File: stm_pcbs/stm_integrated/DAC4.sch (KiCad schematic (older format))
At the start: 21 parts, among them P4 BNC, U10 AD8676, U11 AD5791, U12 AD8675

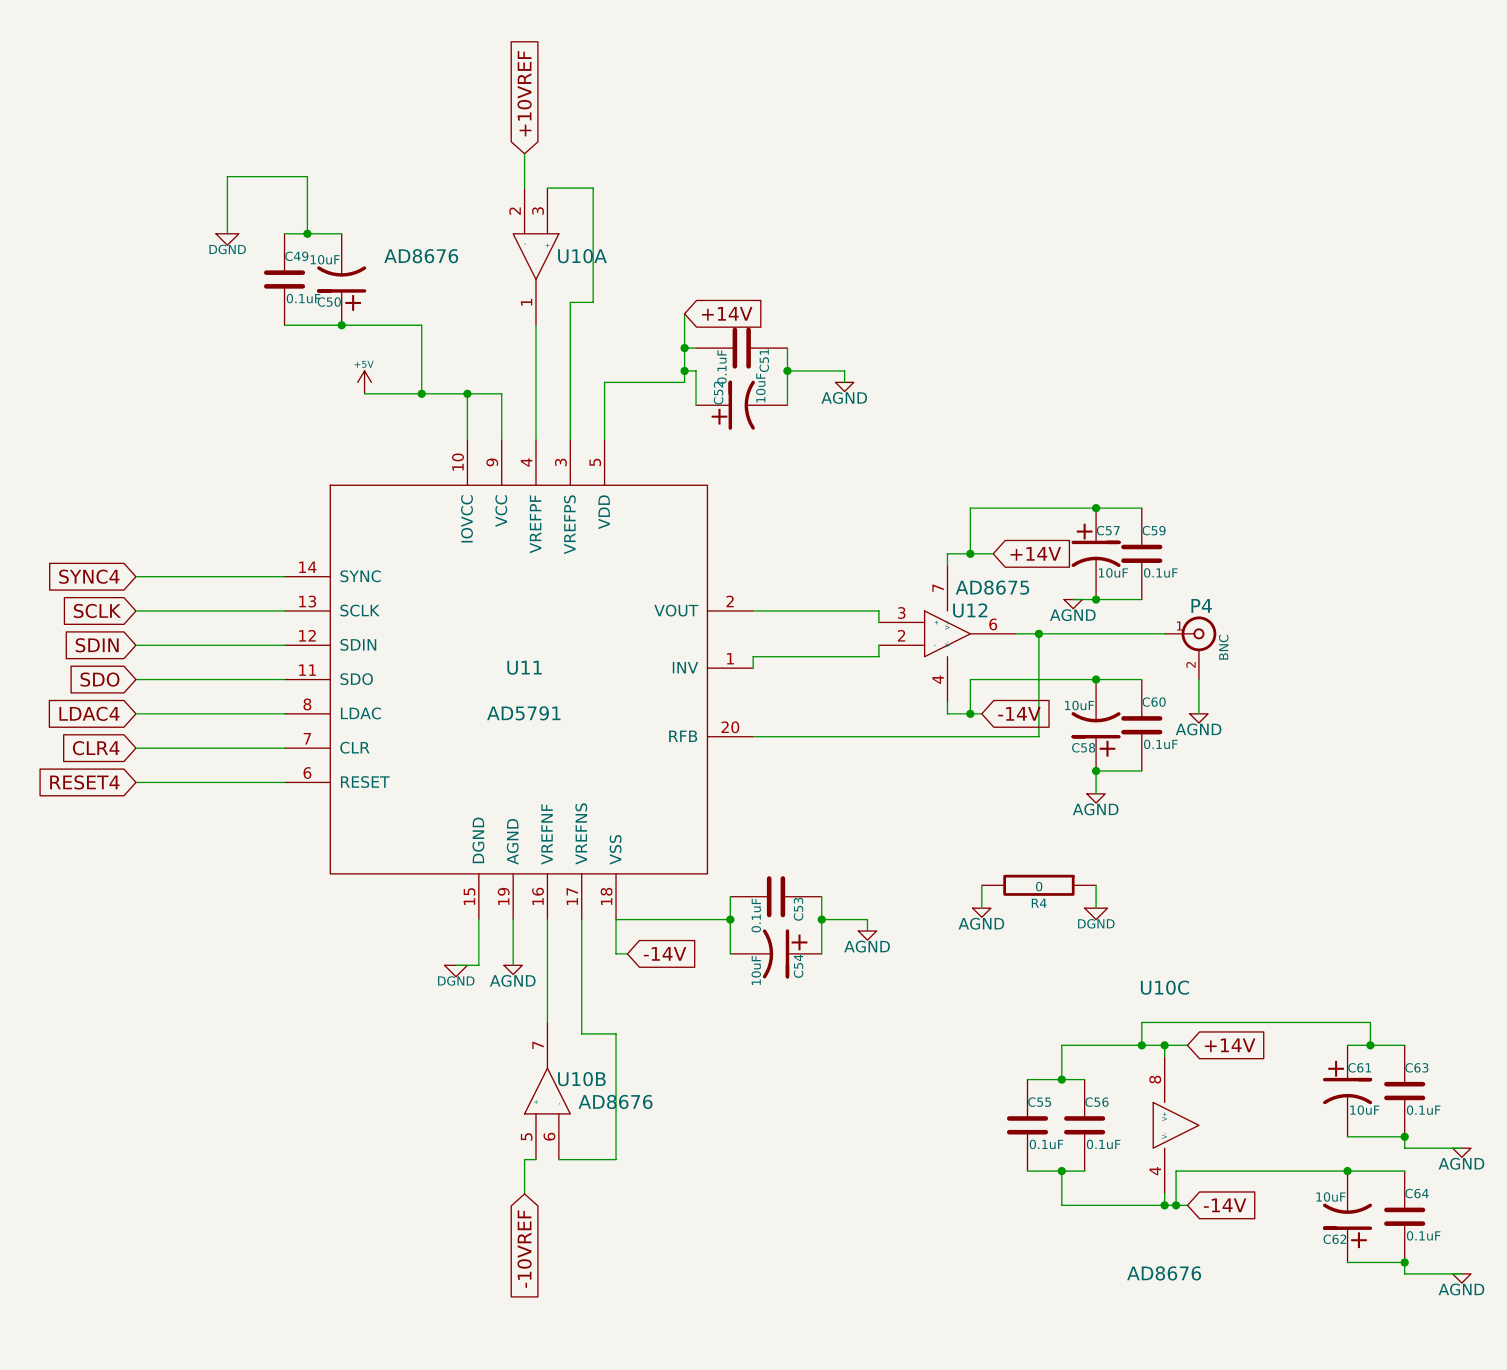
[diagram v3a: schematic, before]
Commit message: fixed issue with DAC (opamp wiring was wrong)
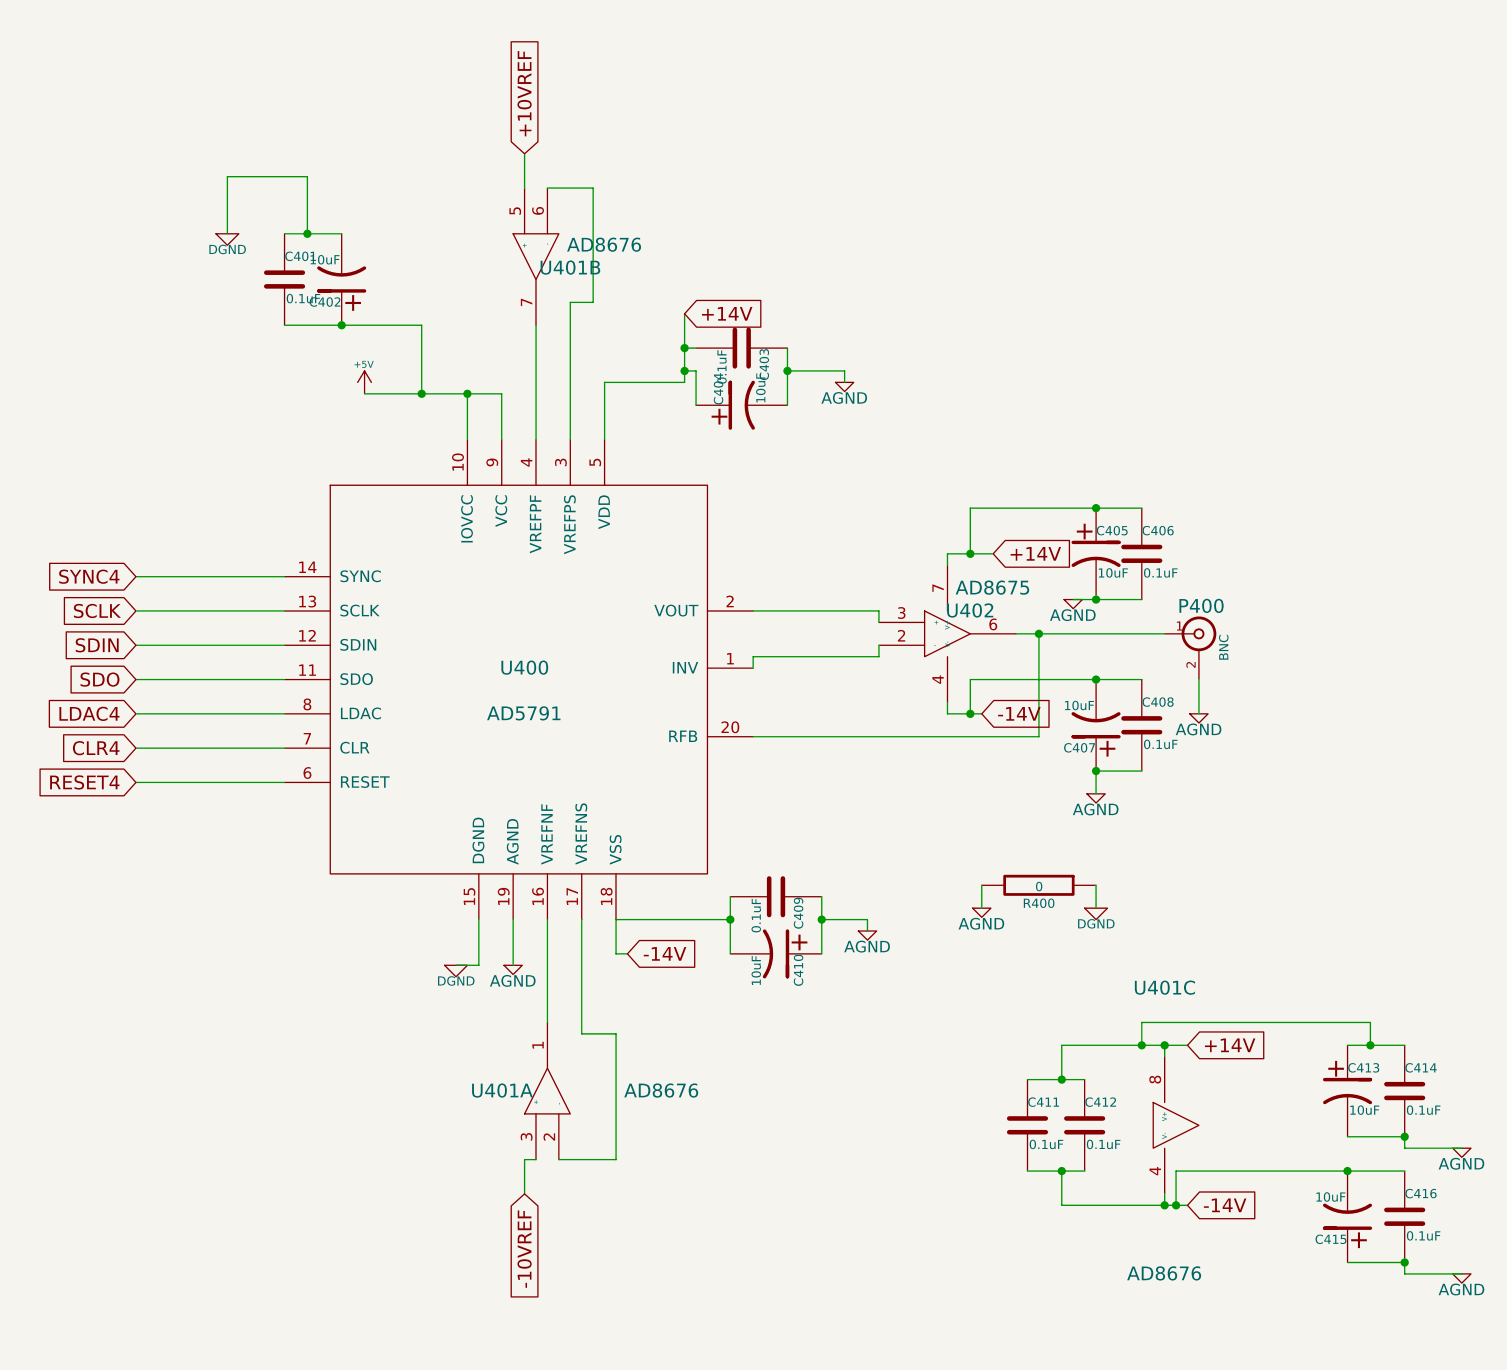
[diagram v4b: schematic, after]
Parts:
- renumbered C49 to C401, C50 to C402, C51 to C403, C52 to C404, C57 to C405, C59 to C406, C58 to C407, C60 to C408, C53 to C409, C54 to C410, C55 to C411, C56 to C412, C61 to C413, C63 to C414, C62 to C415, C64 to C416, P4 to P400, R4 to R400, U11 to U400, U10 to U401, U12 to U402
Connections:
- net +10VREF: now also U401.5 (+); no longer U401.2 (-)
- net -10VREF: now also U401.3 (+); no longer U401.5 (+)
- net at U400.16 (VREFNF): now also U401.1; no longer U401.7
- net at U400.17 (VREFNS): now also U401.2 (-); no longer U401.6 (-)
- net at U400.3 (VREFPS): now also U401.6 (-); no longer U401.3 (+)
- net at U400.4 (VREFPF): now also U401.7; no longer U401.1
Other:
- moved on the sheet: U401A, U401B
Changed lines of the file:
@@
 $EndDescr
 $Comp
-L ad5791:AD5791 U11
+L ad5791:AD5791 U400
 U 1 1 5A26063E
 P 5150 3800
-F 0 "U11" H 5000 4000 60  0000 C CNN
+F 0 "U400" H 5000 4000 60  0000 C CNN
 F 1 "AD5791" H 5000 3800 60  0000 C CNN
 F 2 "stm:SSOP-20" H 5150 3850 60  0001 C CNN
@@
 $EndComp
 $Comp
-L ad5791:AD8675 U12
+L ad5791:AD8675 U402
 U 1 1 5A260645
 P 6850 3450
-F 0 "U12" H 6950 3550 60  0000 C CNN
+F 0 "U402" H 6950 3550 60  0000 C CNN
 F 1 "AD8675" H 7050 3650 60  0000 C CNN
 F 2 "stm:SOIC-8" H 7050 3400 60  0001 C CNN
@@
 $EndComp
 $Comp
-L ad5791:AD8676 U10
+L ad5791:AD8676 U401
 U 1 1 5A26064C
+P 5100 5500
+F 0 "U401" V 5150 5700 60  0000 C CNN
+F 1 "AD8676" V 5150 5000 60  0000 C CNN
+F 2 "stm:SOIC-8" H 5250 5500 60  0001 C CNN
+F 3 "" H 5250 5500 60  0000 C CNN
+	1    5100 5500
+	0    -1   -1   0
+$EndComp
+$Comp
+L ad5791:AD8676 U401
+U 2 1 5A260653
 P 5050 1750
-F 0 "U10" V 5100 1950 60  0000 C CNN
-F 1 "AD8676" V 5100 1250 60  0000 C CNN
+F 0 "U401" V 5150 1600 60  0000 C CNN
+F 1 "AD8676" V 5050 1450 60  0000 C CNN
 F 2 "stm:SOIC-8" H 5200 1750 60  0001 C CNN
 F 3 "" H 5200 1750 60  0000 C CNN
-	1    5050 1750
-	0    1    1    0
-$EndComp
-$Comp
-L ad5791:AD8676 U10
-U 2 1 5A260653
-P 5100 5500
-F 0 "U10" V 5200 5350 60  0000 C CNN
-F 1 "AD8676" V 5100 5200 60  0000 C CNN
-F 2 "stm:SOIC-8" H 5250 5500 60  0001 C CNN
-F 3 "" H 5250 5500 60  0000 C CNN
-	2    5100 5500
-	0    -1   -1   0
-$EndComp
-$Comp
-L ad5791:AD8676 U10
+	2    5050 1750
+	0    -1   1    0
+$EndComp
+$Comp
+L ad5791:AD8676 U401
 U 3 1 5A26065A
 P 7800 5600
-F 0 "U10" H 7800 6200 60  0000 C CNN
+F 0 "U401" H 7800 6200 60  0000 C CNN
 F 1 "AD8676" H 7800 4950 60  0000 C CNN
 F 2 "stm:SOIC-8" H 7950 5600 60  0001 C CNN
@@
 $EndComp
 $Comp
-L device:BNC P4
+L device:BNC P400
 U 1 1 5A260661
 P 7950 3450
-F 0 "P4" H 7960 3570 60  0000 C CNN
+F 0 "P400" H 7960 3570 60  0000 C CNN
 F 1 "BNC" V 8060 3390 40  0000 C CNN
 F 2 "stm:SMA" H 7950 3450 60  0001 C CNN
@@
 $EndComp
 $Comp
-L device:C C51
+L device:C C403
 U 1 1 5A260683
 P 5950 2200
-F 0 "C51" H 5950 2300 40  0000 L CNN
+F 0 "C403" H 5950 2300 40  0000 L CNN
 F 1 "0.1uF" H 5956 2115 40  0000 L CNN
 F 2 "Capacitors_SMD:C_0805_HandSoldering" H 5988 2050 30  0001 C CNN
@@
 $EndComp
 $Comp
-L device:C C53
+L device:C C409
 U 1 1 5A260690
 P 6100 4600
-F 0 "C53" H 6100 4700 40  0000 L CNN
+F 0 "C409" H 6100 4700 40  0000 L CNN
 F 1 "0.1uF" H 6106 4515 40  0000 L CNN
 F 2 "Capacitors_SMD:C_0805_HandSoldering" H 6138 4450 30  0001 C CNN
@@
 $EndComp
 $Comp
-L device:C C49
+L device:C C401
 U 1 1 5A2606AB
 P 3950 1900
-F 0 "C49" H 3950 2000 40  0000 L CNN
+F 0 "C401" H 3950 2000 40  0000 L CNN
 F 1 "0.1uF" H 3956 1815 40  0000 L CNN
 F 2 "Capacitors_SMD:C_0805_HandSoldering" H 3988 1750 30  0001 C CNN
@@
 $EndComp
 $Comp
-L device:C C56
+L device:C C412
 U 1 1 5A2606B8
 P 7450 5600
-F 0 "C56" H 7450 5700 40  0000 L CNN
+F 0 "C412" H 7450 5700 40  0000 L CNN
 F 1 "0.1uF" H 7456 5515 40  0000 L CNN
 F 2 "Capacitors_SMD:C_0805_HandSoldering" H 7488 5450 30  0001 C CNN
@@
 $EndComp
 $Comp
-L device:C C63
+L device:C C414
 U 1 1 5A2606BF
 P 8850 5450
-F 0 "C63" H 8850 5550 40  0000 L CNN
+F 0 "C414" H 8850 5550 40  0000 L CNN
 F 1 "0.1uF" H 8856 5365 40  0000 L CNN
 F 2 "Capacitors_SMD:C_0805_HandSoldering" H 8888 5300 30  0001 C CNN
@@
 $EndComp
 $Comp
-L device:C C64
+L device:C C416
 U 1 1 5A2606C6
 P 8850 6000
-F 0 "C64" H 8850 6100 40  0000 L CNN
+F 0 "C416" H 8850 6100 40  0000 L CNN
 F 1 "0.1uF" H 8856 5915 40  0000 L CNN
 F 2 "Capacitors_SMD:C_0805_HandSoldering" H 8888 5850 30  0001 C CNN
@@
 $EndComp
 $Comp
-L device:C C55
+L device:C C411
 U 1 1 5A2606D9
 P 7200 5600
-F 0 "C55" H 7200 5700 40  0000 L CNN
+F 0 "C411" H 7200 5700 40  0000 L CNN
 F 1 "0.1uF" H 7206 5515 40  0000 L CNN
 F 2 "Capacitors_SMD:C_0805_HandSoldering" H 7238 5450 30  0001 C CNN
@@
 $EndComp
 $Comp
-L device:CP1 C61
+L device:CP1 C413
 U 1 1 5A2606E0
 P 8600 5450
-F 0 "C61" H 8600 5550 40  0000 L CNN
+F 0 "C413" H 8600 5550 40  0000 L CNN
 F 1 "10uF" H 8606 5365 40  0000 L CNN
 F 2 "stm:SMD-1210_Pol" H 8638 5300 30  0001 C CNN
@@
 $EndComp
 $Comp
-L device:CP1 C62
+L device:CP1 C415
 U 1 1 5A2606E7
 P 8600 6000
-F 0 "C62" H 8600 6100 40  0000 L CNN
+F 0 "C415" H 8600 6100 40  0000 L CNN
 F 1 "10uF" H 8606 5915 40  0000 L CNN
 F 2 "stm:SMD-1210_Pol" H 8638 5850 30  0001 C CNN
@@
 $EndComp
 $Comp
-L device:CP1 C54
+L device:CP1 C410
 U 1 1 5A2606EE
 P 6100 4850
-F 0 "C54" H 6100 4950 40  0000 L CNN
+F 0 "C410" H 6100 4950 40  0000 L CNN
 F 1 "10uF" H 6106 4765 40  0000 L CNN
 F 2 "stm:SMD-1210_Pol" H 6138 4700 30  0001 C CNN
@@
 $EndComp
 $Comp
-L device:CP1 C52
+L device:CP1 C404
 U 1 1 5A2606F5
 P 5950 2450
-F 0 "C52" H 5950 2550 40  0000 L CNN
+F 0 "C404" H 5950 2550 40  0000 L CNN
 F 1 "10uF" H 5956 2365 40  0000 L CNN
 F 2 "stm:SMD-1210_Pol" H 5988 2300 30  0001 C CNN
@@
 $EndComp
 $Comp
-L device:CP1 C50
+L device:CP1 C402
 U 1 1 5A2606FC
 P 4200 1900
-F 0 "C50" H 4200 2000 40  0000 L CNN
+F 0 "C402" H 4200 2000 40  0000 L CNN
 F 1 "10uF" H 4206 1815 40  0000 L CNN
 F 2 "stm:SMD-1210_Pol" H 4238 1750 30  0001 C CNN
@@
 RESET4
 $Comp
-L device:CP1 C57
+L device:CP1 C405
 U 1 1 5A26070A
 P 7500 3100
-F 0 "C57" H 7500 3200 40  0000 L CNN
+F 0 "C405" H 7500 3200 40  0000 L CNN
 F 1 "10uF" H 7506 3015 40  0000 L CNN
 F 2 "stm:SMD-1210_Pol" H 7538 2950 30  0001 C CNN
@@
 $EndComp
 $Comp
-L device:CP1 C58
+L device:CP1 C407
 U 1 1 5A260711
 P 7500 3850
-F 0 "C58" H 7500 3950 40  0000 L CNN
+F 0 "C407" H 7500 3950 40  0000 L CNN
 F 1 "10uF" H 7506 3765 40  0000 L CNN
 F 2 "stm:SMD-1210_Pol" H 7538 3700 30  0001 C CNN
@@
 $EndComp
 $Comp
-L device:C C59
+L device:C C406
 U 1 1 5A260718
 P 7700 3100
-F 0 "C59" H 7700 3200 40  0000 L CNN
+F 0 "C406" H 7700 3200 40  0000 L CNN
 F 1 "0.1uF" H 7706 3015 40  0000 L CNN
 F 2 "Capacitors_SMD:C_0805_HandSoldering" H 7738 2950 30  0001 C CNN
@@
 $EndComp
 $Comp
-L device:C C60
+L device:C C408
 U 1 1 5A26071F
 P 7700 3850
-F 0 "C60" H 7700 3950 40  0000 L CNN
+F 0 "C408" H 7700 3950 40  0000 L CNN
 F 1 "0.1uF" H 7706 3765 40  0000 L CNN
 F 2 "Capacitors_SMD:C_0805_HandSoldering" H 7738 3700 30  0001 C CNN
@@
 Connection ~ 6950 3800
 $Comp
-L device:R R4
+L device:R R400
 U 1 1 5A2607A6
 P 7250 4550
-F 0 "R4" V 7330 4550 40  0000 C CNN
+F 0 "R400" V 7330 4550 40  0000 C CNN
 F 1 "0" V 7257 4551 40  0000 C CNN
 F 2 "stm:0Ohm" V 7180 4550 30  0001 C CNN
